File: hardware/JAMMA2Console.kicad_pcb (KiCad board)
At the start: 2 copper layers, 138 x 105 mm, 175 parts, among them J1 Conn_02x28_JAMMA, J10 Conn_02x03_Counter_Clockwise, J11 Conn_02x05_Odd_Even, J2 DB15_Female_HighDensity, J3 SCART-F, J4 DF1BZ-34DP-2.5DSA, J5 Conn_Coaxial_x2, J6 DB15_Female, J7 DB15_Female, J8 Phoenix PTS 1,5/4-5.0, J9 USB_B, U1 USBLC6-2P6, U10 74LVC4245, U11 74LVC4245, U12 TL074, U13 LM1972, U14 TPA3138D2, U15 74HCT4053, U2 LD1117-3.3, U3 74HCT4053, U4 74HCT86, U5 74HCT4053, U6 LM1881, U7 THS7375, U8 STM32F103V8Tx, U9 74LVC4245, Y1 8MHz

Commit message: Completing the functionality of PCB layout. Require silkscreen placement still, though.
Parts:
- removed RN10, RN14, RN3, RN7, RN8, RN9: 10k, Resistor_SMD:R_Array_Convex_4x0603
- added C70: 100n, Capacitor_SMD:C_0603_1608Metric, F.Cu at (157.2, 133.8)
- added C71: 100n, Capacitor_SMD:C_0603_1608Metric, F.Cu at (157.2, 149.7)
- added D7: LESD3Z5.0CMT1G, Diode_SMD:D_SOD-323, F.Cu at (52.9, 157.3)
- added J12: Conn_01x03, Connector_PinHeader_2.54mm:PinHeader_1x03_P2.54mm_Vertical, F.Cu at (106.6, 139.9)
- added JP3: Jumper_NC_Small, Jumper:SolderJumper-2_P1.3mm_Bridged2Bar_Pad1.0x1.5mm, F.Cu at (102.9, 142.5)
- added R30: 1K5, Resistor_SMD:R_0603_1608Metric, F.Cu at (57.6, 156.8)
- added R31: 10K, Resistor_SMD:R_0603_1608Metric, F.Cu at (111.0, 140.7)
- added R32: 10K, Resistor_SMD:R_0603_1608Metric, F.Cu at (123.9, 140.7)
- added R33: 10K, Resistor_SMD:R_0603_1608Metric, F.Cu at (137.0, 140.8)
- added R34: 10K, Resistor_SMD:R_0603_1608Metric, F.Cu at (159.5, 133.0)
- added R35: 10K, Resistor_SMD:R_0603_1608Metric, F.Cu at (159.4, 148.9)
- added R36: 10K, Resistor_SMD:R_Array_Convex_4x0603, F.Cu at (100.9, 104.8)
- added R37: 10K, Resistor_SMD:R_Array_Convex_4x0603, F.Cu at (81.2, 124.7)
- added R38: 10K, Resistor_SMD:R_Array_Convex_4x0603, F.Cu at (85.6, 125.0)
- added R39: 10K, Resistor_SMD:R_Array_Convex_4x0603, F.Cu at (148.5, 99.8)
- added R40: 10K, Resistor_SMD:R_0603_1608Metric, F.Cu at (157.2, 132.2)
- added R41: 10K, Resistor_SMD:R_0603_1608Metric, F.Cu at (157.2, 148.2)
- added R42: 10K, Resistor_SMD:R_0603_1608Metric, F.Cu at (99.2, 126.7)
- added R43: 10K, Resistor_SMD:R_0603_1608Metric, F.Cu at (88.2, 125.0)
- added SW1: SW_Push, Console2JAMMA:SW_Push_SPST_NO_Alps_SKRP, F.Cu at (110.0, 98.8)
- added SW2: SW_Push, Console2JAMMA:SW_Push_SPST_NO_Alps_SKRP, F.Cu at (157.5, 128.5)
- added SW3: SW_Push, Console2JAMMA:SW_Push_SPST_NO_Alps_SKRP, F.Cu at (157.5, 144.5)
- J2: value DB15_Female_HighDensity -> DS1038-15FBNSiA74-0CC; footprint Connector_Dsub:DSUB-15-HD_Female_Horizontal_P2.29x1.98mm_EdgePinOffset8.35mm_Housed_MountingHolesOffset10.89mm -> Console2JAMMA:DSUB-15-HD_Female_Horizontal_P2.29x1.98mm_EdgePinOffset8.63mm_Housed_MountingHolesOffset11.17mm
- J3: footprint Console2JAMMA:Conn_SCART_Female -> Console2JAMMA:Conn_SCART_Female_Right_Angle
- J5: value Conn_Coaxial_x2 -> AudioJack3; footprint Console2JAMMA:RCA_Switchchraft_Dual -> Connector_Audio:Jack_3.5mm_CUI_SJ-3523-SMT_Horizontal
- J6, J7: value DB15_Female -> DS1037-15FNAKT74-0CC; footprint Connector_Dsub:DSUB-15_Female_Horizontal_P2.77x2.84mm_EdgePinOffset7.70mm_Housed_MountingHolesOffset9.12mm -> Console2JAMMA:DSUB-15_Female_Horizontal_P2.77x2.84mm_EdgePinOffset8.10mm_Housed_MountingHolesOffset9.52mm
- J9: value USB_B -> USB_B_Mini; footprint Connector_USB:USB_B_OST_USB-B1HSxx_Horizontal -> Connector_USB:USB_Mini-B_Lumberg_2486_01_Horizontal
- R9: value 10K -> 680K
- Y1: value 8MHz -> 12MHz
- moved R9 305.0 mm to (45.2, 159.2), turned to 180 degrees
- moved C16 262.2 mm to (80.6, 108.7), turned to 90 degrees
- moved C24 243.1 mm to (94.2, 104.5)
- moved C25 239.9 mm to (101.7, 108.3), turned to 270 degrees
- moved C23 238.5 mm to (98.5, 123.8), turned to 180 degrees
- moved C22 237.6 mm to (82.0, 121.2), turned to 90 degrees
- moved C17 234.3 mm to (86.4, 101.7), turned to 180 degrees
- moved C31 234.2 mm to (111.0, 137.6), turned to 270 degrees
- moved RN18 231.5 mm to (115.5, 144.5), turned to 90 degrees
- moved C21 230.9 mm to (82.3, 108.8), turned to 90 degrees
- moved C34 228.6 mm to (112.5, 140.7), turned to 90 degrees
- moved C35 227.1 mm to (125.4, 140.7), turned to 90 degrees
- moved C28 224.7 mm to (112.5, 137.7), turned to 270 degrees
- moved RN21 223.5 mm to (132.5, 144.5), turned to 90 degrees
- moved C20 222.2 mm to (86.4, 103.3), turned to 180 degrees
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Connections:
- net /Audio/Audio_L_Mono renamed /Audio/Audio_~Mono~_L
- net Net-(J9-Pad2) renamed /D-
- net Net-(J9-Pad3) renamed /D+
- C14 pad 1: +3V3 -> +5V
- C15 pad 1: +3V3 -> +5V
- C66 pad 1: /Speaker_JAMMA+ -> /Speaker_JAMMA-
- C67 pad 2: /Speaker_JAMMA- -> /Speaker_JAMMA+
- D8 pad 1: /VGA_HSYNC -> GND
- D8 pad 2: GND -> /VGA_HSYNC
- D9 pad 1: /VGA_VSYNC -> GND
- D9 pad 2: GND -> /VGA_VSYNC
- J2 pad 0: (no net) -> GND
- J6 pad 0: (no net) -> GND
- J6 pad 1: /Digital I/O/VCC -> Net-(J6-Pad1)
- J6 pad 10: /Digital I/O/P1_3 -> /Digital I/O/P1_2
- J6 pad 11: /Digital I/O/P1_5 -> /Digital I/O/P1_4
- J6 pad 12: /Digital I/O/P1_7 -> /Digital I/O/P1_6
- J6 pad 13: /Digital I/O/P1_9 -> /Digital I/O/P1_8
- J6 pad 14: /Digital I/O/P1_11 -> /Digital I/O/P1_10
- J6 pad 15: GND -> /Digital I/O/P1_12
- J6 pad 2: /Digital I/O/P1_2 -> /Digital I/O/P1_1
- J6 pad 3: /Digital I/O/P1_4 -> /Digital I/O/P1_3
- J6 pad 4: /Digital I/O/P1_6 -> /Digital I/O/P1_5
- J6 pad 5: /Digital I/O/P1_8 -> /Digital I/O/P1_7
- J6 pad 6: /Digital I/O/P1_10 -> /Digital I/O/P1_9
- J6 pad 7: /Digital I/O/P1_12 -> /Digital I/O/P1_11
- J6 pad 9: /Digital I/O/P1_1 -> Net-(J6-Pad9)
- J7 pad 0: (no net) -> GND
- J7 pad 1: /Digital I/O/VCC -> Net-(J6-Pad1)
- J7 pad 10: /Digital I/O/P2_3 -> /Digital I/O/P2_2
- J7 pad 11: /Digital I/O/P2_5 -> /Digital I/O/P2_4
- J7 pad 12: /Digital I/O/P2_7 -> /Digital I/O/P2_6
- J7 pad 13: /Digital I/O/P2_9 -> /Digital I/O/P2_8
- J7 pad 14: /Digital I/O/P2_11 -> /Digital I/O/P2_10
- J7 pad 15: GND -> /Digital I/O/P2_12
- J7 pad 2: /Digital I/O/P2_2 -> /Digital I/O/P2_1
- J7 pad 3: /Digital I/O/P2_4 -> /Digital I/O/P2_3
- J7 pad 4: /Digital I/O/P2_6 -> /Digital I/O/P2_5
- J7 pad 5: /Digital I/O/P2_8 -> /Digital I/O/P2_7
- J7 pad 6: /Digital I/O/P2_10 -> /Digital I/O/P2_9
- J7 pad 7: /Digital I/O/P2_12 -> /Digital I/O/P2_11
- J7 pad 9: /Digital I/O/P2_1 -> Net-(J7-Pad9)
- J8 pad 1: /Audio/Speaker_R+ -> /Speaker_JAMMA+
- J8 pad 2: /Audio/Speaker_R- -> /Speaker_JAMMA-
- J8 pad 3: /Speaker_JAMMA- -> /Audio/Speaker_R+
- J8 pad 4: /Speaker_JAMMA+ -> /Audio/Speaker_R-
- J9 pad 4: GND -> Net-(J9-Pad4)
- JP1 pad 3: +3V3 -> +12V
- JP2 pad 3: +3V3 -> +12V
- L1 pad 2: /Speaker_JAMMA+ -> /Speaker_JAMMA-
- L2 pad 2: /Speaker_JAMMA- -> /Speaker_JAMMA+
- R26 pad 1: +3V3 -> +12V
- R9 pad 1: +3V3 -> Net-(J9-Pad6)
- R9 pad 2: Net-(R9-Pad2) -> GND
- RN1 pad 5: /Video/Video_CSYNC -> /Video/Video_Green
- RN1 pad 6: /Video/Video_Blue -> /Video/Video_Red
- RN1 pad 7: /Video/Video_Green -> /Video/Video_CSYNC
- RN1 pad 8: /Video/Video_Red -> /Video/Video_Blue
- RN11 pad 1: /Digital I/O/P1_Shifter_DIR -> Net-(RN11-Pad1)
- RN11 pad 2: /Digital I/O/P1_Button1 -> Net-(RN11-Pad2)
- RN11 pad 3: /Digital I/O/P1_Button2 -> Net-(RN11-Pad3)
- RN11 pad 4: /Digital I/O/P1_Button3 -> Net-(RN11-Pad4)
- RN11 pad 5: Net-(RN11-Pad5) -> /Digital I/O/P1_Button4
- RN11 pad 6: Net-(RN11-Pad6) -> /Digital I/O/P1_Button3
- RN11 pad 7: Net-(RN11-Pad7) -> /Digital I/O/P1_Button2
- RN11 pad 8: Net-(RN11-Pad8) -> /Digital I/O/P1_Button1
- RN12 pad 1: /Digital I/O/P1_Button4 -> Net-(RN12-Pad1)
- RN12 pad 2: /Digital I/O/P1_Button5 -> Net-(RN12-Pad2)
- RN12 pad 3: /Digital I/O/P1_Button6 -> Net-(RN12-Pad3)
- RN12 pad 4: /Digital I/O/P1_Button7 -> Net-(RN12-Pad4)
- RN12 pad 5: Net-(RN12-Pad5) -> /Digital I/O/P1_Button8
- RN12 pad 6: Net-(RN12-Pad6) -> /Digital I/O/P1_Button7
- RN12 pad 7: Net-(RN12-Pad7) -> /Digital I/O/P1_Button6
- RN12 pad 8: Net-(RN12-Pad8) -> /Digital I/O/P1_Button5
- RN13 pad 1: /Digital I/O/P1_Button8 -> Net-(RN13-Pad1)
- RN13 pad 2: /Digital I/O/P1&P2_Shifter_DIR -> Net-(RN13-Pad2)
- RN13 pad 3: /Digital I/O/P1_Button9 -> Net-(RN13-Pad3)
- RN13 pad 4: /Digital I/O/P1_Button10 -> Net-(RN13-Pad4)
- RN13 pad 5: Net-(RN13-Pad5) -> /Digital I/O/P1_Button12
- RN13 pad 6: Net-(RN13-Pad6) -> /Digital I/O/P1_Button11
- RN13 pad 7: Net-(RN13-Pad7) -> /Digital I/O/P1_Button10
- RN13 pad 8: Net-(RN13-Pad8) -> /Digital I/O/P1_Button9
- RN15 pad 1: /Digital I/O/P2_Button11 -> Net-(RN15-Pad1)
- RN15 pad 2: /Digital I/O/P2_Button12 -> Net-(RN15-Pad2)
- RN15 pad 3: /Digital I/O/P2_Shifter_DIR -> Net-(RN15-Pad3)
- RN15 pad 4: /Digital I/O/P2_Button1 -> Net-(RN15-Pad4)
- RN15 pad 5: Net-(RN15-Pad5) -> /Digital I/O/P2_Button4
- RN15 pad 6: Net-(RN15-Pad6) -> /Digital I/O/P2_Button3
- RN15 pad 7: Net-(RN15-Pad7) -> /Digital I/O/P2_Button2
- RN15 pad 8: Net-(RN15-Pad8) -> /Digital I/O/P2_Button1
- RN16 pad 1: /Digital I/O/P2_Button2 -> Net-(RN16-Pad1)
- RN16 pad 2: /Digital I/O/P2_Button3 -> Net-(RN16-Pad2)
- RN16 pad 3: /Digital I/O/P2_Button4 -> Net-(RN16-Pad3)
- RN16 pad 4: /Digital I/O/P2_Button5 -> Net-(RN16-Pad4)
- RN16 pad 5: Net-(RN16-Pad5) -> /Digital I/O/P2_Button8
- RN16 pad 6: Net-(RN16-Pad6) -> /Digital I/O/P2_Button7
- RN16 pad 7: Net-(RN16-Pad7) -> /Digital I/O/P2_Button6
- RN16 pad 8: Net-(RN16-Pad8) -> /Digital I/O/P2_Button5
- RN17 pad 1: /Digital I/O/P2_Button6 -> Net-(RN17-Pad1)
- RN17 pad 2: /Digital I/O/P2_Button7 -> Net-(RN17-Pad2)
- RN17 pad 3: /Digital I/O/P2_Button8 -> Net-(RN17-Pad3)
- RN17 pad 5: Net-(RN17-Pad5) -> /Digital I/O/P2_Button12
- RN17 pad 6: Net-(RN17-Pad6) -> /Digital I/O/P2_Button11
- RN17 pad 7: Net-(RN17-Pad7) -> /Digital I/O/P2_Button10
- RN17 pad 8: Net-(RN17-Pad8) -> /Digital I/O/P2_Button9
- RN18 pad 1: Net-(RN18-Pad1) -> /Digital I/O/P1_1
- RN18 pad 2: Net-(RN18-Pad2) -> /Digital I/O/P1_2
- RN18 pad 3: Net-(RN18-Pad3) -> /Digital I/O/P1_3
- RN18 pad 4: Net-(RN18-Pad4) -> /Digital I/O/P1_4
- RN18 pad 5: /Digital I/O/P1_4 -> Net-(RN18-Pad5)
- RN18 pad 6: /Digital I/O/P1_3 -> Net-(RN18-Pad6)
- RN18 pad 7: /Digital I/O/P1_2 -> Net-(RN18-Pad7)
- RN18 pad 8: /Digital I/O/P1_1 -> Net-(RN18-Pad8)
- RN19 pad 1: Net-(RN19-Pad1) -> /Digital I/O/P1_5
- RN19 pad 2: Net-(RN19-Pad2) -> /Digital I/O/P1_6
- RN19 pad 3: Net-(RN19-Pad3) -> /Digital I/O/P1_7
- RN19 pad 4: Net-(RN19-Pad4) -> /Digital I/O/P1_8
- RN19 pad 5: /Digital I/O/P1_8 -> Net-(RN19-Pad5)
- RN19 pad 6: /Digital I/O/P1_7 -> Net-(RN19-Pad6)
- RN19 pad 7: /Digital I/O/P1_6 -> Net-(RN19-Pad7)
- RN19 pad 8: /Digital I/O/P1_5 -> Net-(RN19-Pad8)
- RN2 pad 5: /Composite_Sync -> /Video_Green
- RN2 pad 6: /Video_Blue -> /Video_Red
- RN2 pad 7: /Video_Green -> /Composite_Sync
- RN2 pad 8: /Video_Red -> /Video_Blue
- RN20 pad 1: Net-(RN20-Pad1) -> /Digital I/O/P1_9
- RN20 pad 2: Net-(RN20-Pad2) -> /Digital I/O/P1_10
- RN20 pad 3: Net-(RN20-Pad3) -> /Digital I/O/P1_11
- RN20 pad 4: Net-(RN20-Pad4) -> /Digital I/O/P1_12
- RN20 pad 5: /Digital I/O/P1_12 -> Net-(RN20-Pad5)
- RN20 pad 6: /Digital I/O/P1_11 -> Net-(RN20-Pad6)
- RN20 pad 7: /Digital I/O/P1_10 -> Net-(RN20-Pad7)
- RN20 pad 8: /Digital I/O/P1_9 -> Net-(RN20-Pad8)
- RN21 pad 1: Net-(RN21-Pad1) -> /Digital I/O/P2_1
- RN21 pad 2: Net-(RN21-Pad2) -> /Digital I/O/P2_2
- RN21 pad 3: Net-(RN21-Pad3) -> /Digital I/O/P2_3
- RN21 pad 4: Net-(RN21-Pad4) -> /Digital I/O/P2_4
- RN21 pad 5: /Digital I/O/P2_12 -> Net-(RN21-Pad5)
- RN21 pad 6: /Digital I/O/P2_11 -> Net-(RN21-Pad6)
- RN21 pad 7: /Digital I/O/P2_10 -> Net-(RN21-Pad7)
- RN21 pad 8: /Digital I/O/P2_9 -> Net-(RN21-Pad8)
- RN22 pad 1: Net-(RN22-Pad1) -> /Digital I/O/P2_5
- RN22 pad 2: Net-(RN22-Pad2) -> /Digital I/O/P2_6
- RN22 pad 3: Net-(RN22-Pad3) -> /Digital I/O/P2_7
- RN22 pad 4: Net-(RN22-Pad4) -> /Digital I/O/P2_8
- RN22 pad 5: /Digital I/O/P2_4 -> Net-(RN22-Pad5)
- RN22 pad 6: /Digital I/O/P2_3 -> Net-(RN22-Pad6)
- RN22 pad 7: /Digital I/O/P2_2 -> Net-(RN22-Pad7)
- RN22 pad 8: /Digital I/O/P2_1 -> Net-(RN22-Pad8)
- RN23 pad 1: Net-(RN23-Pad1) -> /Digital I/O/P2_9
- RN23 pad 2: Net-(RN23-Pad2) -> /Digital I/O/P2_10
- RN23 pad 3: Net-(RN23-Pad3) -> /Digital I/O/P2_11
- RN23 pad 4: Net-(RN23-Pad4) -> /Digital I/O/P2_12
- RN23 pad 5: /Digital I/O/P2_8 -> Net-(RN23-Pad5)
- RN23 pad 6: /Digital I/O/P2_7 -> Net-(RN23-Pad6)
- RN23 pad 7: /Digital I/O/P2_6 -> Net-(RN23-Pad7)
- RN23 pad 8: /Digital I/O/P2_5 -> Net-(RN23-Pad8)
- RN4 pad 1: /P1_Down -> /P1_Start
- RN4 pad 2: /P1_Left -> /P2_Up
- RN4 pad 3: /P1_Right -> /P1_Up
- RN4 pad 4: /P1_A -> /P2_Down
- RN5 pad 1: /P1_B -> /P1_Down
- RN5 pad 2: /P1_C -> /P2_Left
- RN5 pad 3: /P1_X -> /P1_Left
- RN5 pad 4: /P1_Y -> /P2_Right
- RN6 pad 1: /P1_Z -> /P1_Right
- RN6 pad 2: /P1_HK -> /P2_A
- RN6 pad 3: /P1_MK -> /P1_A
- RN6 pad 4: /P1_LK -> /P2_B
- U10 pad 10: Net-(RN21-Pad4) -> Net-(RN21-Pad5)
- U10 pad 14: Net-(RN15-Pad7) -> Net-(RN15-Pad4)
- U10 pad 15: Net-(RN15-Pad8) -> Net-(RN15-Pad3)
- U10 pad 16: Net-(RN14-Pad5) -> Net-(RN15-Pad2)
- U10 pad 17: Net-(RN14-Pad6) -> Net-(RN15-Pad1)
- U10 pad 18: Net-(RN14-Pad7) -> Net-(RN13-Pad4)
- U10 pad 19: Net-(RN14-Pad8) -> Net-(RN13-Pad3)
- U10 pad 2: Net-(RN13-Pad7) -> Net-(R32-Pad1)
- U10 pad 20: Net-(RN13-Pad5) -> Net-(RN13-Pad2)
- U10 pad 21: Net-(RN13-Pad6) -> Net-(RN13-Pad1)
- U10 pad 3: Net-(RN20-Pad1) -> Net-(RN20-Pad8)
- U10 pad 4: Net-(RN20-Pad2) -> Net-(RN20-Pad7)
- U10 pad 5: Net-(RN20-Pad3) -> Net-(RN20-Pad6)
- U10 pad 6: Net-(RN20-Pad4) -> Net-(RN20-Pad5)
- U10 pad 7: Net-(RN21-Pad1) -> Net-(RN21-Pad8)
- U10 pad 8: Net-(RN21-Pad2) -> Net-(RN21-Pad7)
- U10 pad 9: Net-(RN21-Pad3) -> Net-(RN21-Pad6)
- U11 pad 10: Net-(RN23-Pad4) -> Net-(RN23-Pad5)
- U11 pad 14: Net-(RN17-Pad6) -> Net-(RN17-Pad4)
- U11 pad 15: Net-(RN17-Pad7) -> Net-(RN17-Pad3)
- U11 pad 16: Net-(RN17-Pad8) -> Net-(RN17-Pad2)
- U11 pad 17: Net-(RN16-Pad5) -> Net-(RN17-Pad1)
- U11 pad 18: Net-(RN16-Pad6) -> Net-(RN16-Pad4)
- U11 pad 19: Net-(RN16-Pad7) -> Net-(RN16-Pad3)
- U11 pad 2: Net-(RN15-Pad6) -> Net-(R33-Pad1)
- U11 pad 20: Net-(RN16-Pad8) -> Net-(RN16-Pad2)
- U11 pad 21: Net-(RN15-Pad5) -> Net-(RN16-Pad1)
- U11 pad 3: Net-(RN22-Pad1) -> Net-(RN22-Pad8)
- U11 pad 4: Net-(RN22-Pad2) -> Net-(RN22-Pad7)
- U11 pad 5: Net-(RN22-Pad3) -> Net-(RN22-Pad6)
- U11 pad 6: Net-(RN22-Pad4) -> Net-(RN22-Pad5)
- U11 pad 7: Net-(RN23-Pad1) -> Net-(RN23-Pad8)
- U11 pad 8: Net-(RN23-Pad2) -> Net-(RN23-Pad7)
- U11 pad 9: Net-(RN23-Pad3) -> Net-(RN23-Pad6)
- U15 pad 3: /Audio/Audio_Mono -> /Audio/Audio_L
- U15 pad 5: /Audio/Audio_L -> /Audio/Audio_Mono
- U3 pad 1: /VGA_Green -> /VGA_Blue
- U3 pad 2: /SCART_Green -> /SCART_Blue
- U3 pad 3: /VGA_Blue -> /VGA_Green
- U3 pad 5: /SCART_Blue -> /SCART_Green
- U4 pad 10: Net-(U4-Pad10) -> +5V
- U4 pad 11: /Video/VGA_CSYNC -> Net-(U4-Pad11)
- U4 pad 12: +5V -> Net-(U4-Pad12)
- U4 pad 3: Net-(U4-Pad3) -> Net-(U4-Pad13)
- U4 pad 6: Net-(U4-Pad10) -> Net-(U4-Pad12)
- U4 pad 8: Net-(U4-Pad13) -> /Video/VGA_CSYNC
- U4 pad 9: Net-(U4-Pad3) -> Net-(U4-Pad11)
- U7 pad 1: /Video/Video_Red -> /Video/Video_Blue
- U7 pad 10: +3V3 -> +5V
- U7 pad 2: /Video/Video_Green -> /Video/Video_CSYNC
- U7 pad 3: /Video/Video_Blue -> /Video/Video_Red
- U7 pad 4: /Video/Video_CSYNC -> /Video/Video_Green
- U8 pad 14: Net-(R9-Pad2) -> Net-(R36-Pad8)
- U8 pad 15: /Digital I/O/P2_Shifter_DIR -> /VOL_DATA_IN
- U8 pad 16: /Digital I/O/P2_Button11 -> /VOL_LOAD_SHIFT
- U8 pad 17: /Digital I/O/P2_Button12 -> /VOL_CLK
- U8 pad 18: /VOL_CLK -> Net-(U8-Pad18)
- U8 pad 23: /Digital I/O/P1_Shifter_DIR -> /Audio_Select_L
- U8 pad 24: /Digital I/O/P1_Button1 -> /Audio_Select_R
- U8 pad 25: /Digital I/O/P1_Button2 -> /Audio_Select_Mono
- U8 pad 26: /Digital I/O/P1_Button3 -> /Video_Select_CSYNC
- U8 pad 29: /Digital I/O/P1_Button4 -> /Video_Select_Green
- U8 pad 30: /Digital I/O/P1_Button5 -> /Video_Select_Blue
- U8 pad 31: /Digital I/O/P1_Button6 -> /Video_Select_Red
- U8 pad 32: /Digital I/O/P1_Button7 -> /Digital I/O/Volume_Down
- U8 pad 33: /VOL_LOAD_SHIFT -> /Digital I/O/Volume_Up
- U8 pad 34: /VOL_DATA_IN -> /Digital I/O/P1_Shifter_DIR
- U8 pad 36: /Digital I/O/P1_Button11 -> /Digital I/O/P2_Shifter_DIR
- U8 pad 47: /Digital I/O/P2_Button5 -> Net-(R37-Pad2)
- U8 pad 48: /Digital I/O/P2_Button6 -> Net-(R37-Pad3)
- U8 pad 51: /Digital I/O/P2_Button7 -> Net-(R37-Pad1)
- U8 pad 52: /Digital I/O/P2_Button8 -> Net-(R38-Pad4)
- U8 pad 53: /Digital I/O/P2_Button9 -> Net-(R38-Pad3)
- U8 pad 54: /Digital I/O/P2_Button10 -> Net-(R38-Pad2)
- U8 pad 57: Net-(RN9-Pad6) -> /Digital I/O/P1_Button1
- U8 pad 58: Net-(RN9-Pad5) -> /Digital I/O/P1_Button2
- U8 pad 59: Net-(RN10-Pad8) -> /Digital I/O/P1_Button3
- U8 pad 6: Net-(U8-Pad6) -> +3V3
- U8 pad 60: Net-(RN10-Pad7) -> /Digital I/O/P1_Button4
- U8 pad 61: Net-(RN10-Pad6) -> /Digital I/O/P1_Button5
- U8 pad 62: Net-(U8-Pad62) -> /Digital I/O/P1_Button6
- U8 pad 63: /Audio_Select_L -> /Digital I/O/P1_Button7
- U8 pad 64: /Audio_Select_R -> /Digital I/O/P1_Button8
- U8 pad 65: /Audio_Select_Mono -> /Digital I/O/P1_Button9
- U8 pad 66: /Video_Select_Red -> /Digital I/O/P1_Button10
- U8 pad 67: /Digital I/O/P1_Button8 -> /Digital I/O/P1_Button11
- U8 pad 68: /Digital I/O/P1_Button9 -> /Digital I/O/P1_Button12
- U8 pad 69: /Digital I/O/P1_Button10 -> /Digital I/O/P2_Button1
- U8 pad 7: Net-(U8-Pad7) -> /P2_LK
- U8 pad 78: /Video_Select_Green -> /Digital I/O/P2_Button2
- U8 pad 79: /Video_Select_Blue -> /Digital I/O/P2_Button3
- U8 pad 8: Net-(U8-Pad8) -> /P2_MK
- U8 pad 80: /Video_Select_CSYNC -> /Digital I/O/P2_Button4
- U8 pad 81: Net-(RN7-Pad8) -> /Digital I/O/P2_Button5
- U8 pad 82: Net-(RN7-Pad7) -> /Digital I/O/P2_Button6
- U8 pad 83: Net-(RN7-Pad6) -> /Digital I/O/P2_Button7
- U8 pad 84: Net-(RN7-Pad5) -> /Digital I/O/P2_Button8
- U8 pad 85: Net-(RN8-Pad8) -> /Digital I/O/P2_Button9
- U8 pad 86: Net-(RN8-Pad7) -> /Digital I/O/P2_Button10
- U8 pad 87: Net-(RN8-Pad6) -> /Digital I/O/P2_Button11
- U8 pad 88: Net-(RN8-Pad5) -> /Digital I/O/USB_Detect
- U8 pad 91: /Digital I/O/P1_Button12 -> /Digital I/O/P2_Button12
- U8 pad 92: /Digital I/O/P2_Button1 -> Net-(R39-Pad4)
- U8 pad 93: /Digital I/O/P2_Button2 -> Net-(R39-Pad3)
- U8 pad 95: /Digital I/O/P2_Button3 -> Net-(R39-Pad2)
- U8 pad 96: /Digital I/O/P2_Button4 -> Net-(R39-Pad1)
- U9 pad 10: Net-(RN19-Pad4) -> Net-(RN19-Pad5)
- U9 pad 14: Net-(RN13-Pad8) -> Net-(RN12-Pad4)
- U9 pad 15: Net-(RN12-Pad5) -> Net-(RN12-Pad3)
- U9 pad 16: Net-(RN12-Pad6) -> Net-(RN12-Pad2)
- U9 pad 17: Net-(RN12-Pad7) -> Net-(RN12-Pad1)
- U9 pad 18: Net-(RN12-Pad8) -> Net-(RN11-Pad4)
- U9 pad 19: Net-(RN11-Pad5) -> Net-(RN11-Pad3)
- U9 pad 2: Net-(RN11-Pad8) -> Net-(R31-Pad1)
- U9 pad 20: Net-(RN11-Pad6) -> Net-(RN11-Pad2)
- U9 pad 21: Net-(RN11-Pad7) -> Net-(RN11-Pad1)
- U9 pad 3: Net-(RN18-Pad1) -> Net-(RN18-Pad8)
- U9 pad 4: Net-(RN18-Pad2) -> Net-(RN18-Pad7)
- U9 pad 5: Net-(RN18-Pad3) -> Net-(RN18-Pad6)
- U9 pad 6: Net-(RN18-Pad4) -> Net-(RN18-Pad5)
- U9 pad 7: Net-(RN19-Pad1) -> Net-(RN19-Pad8)
- U9 pad 8: Net-(RN19-Pad2) -> Net-(RN19-Pad7)
- U9 pad 9: Net-(RN19-Pad3) -> Net-(RN19-Pad6)
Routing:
- net GND: track 87.1 -> 265.9 mm, vias 7 -> 272
- net /P1_B: track 0.00 -> 157.2 mm
- net +5V: track 27.9 -> 169.0 mm, vias 1 -> 35
- net /P1_Z: track 0.00 -> 127.3 mm
- net /Digital I/O/Volume_Up: track 0.00 -> 125.7 mm, vias 0 -> 2
- net /P2_Z: track 0.00 -> 124.6 mm, vias 0 -> 1
- net /P1_Y: track 0.00 -> 120.6 mm
- net /VGA_Green: track 3.70 -> 123.8 mm, vias 0 -> 2
- net /Audio/EXT_Audio_R: track 0.00 -> 119.4 mm, vias 0 -> 4
- net /P2_Y: track 0.00 -> 118.8 mm, vias 0 -> 1
- net /VGA_Red: track 3.70 -> 120.6 mm, vias 0 -> 2
- net /Digital I/O/Volume_Down: track 0.00 -> 115.7 mm, vias 0 -> 2
- net /SCART_Audio_L: track 8.08 -> 123.6 mm, vias 0 -> 4
- net /VGA_Blue: track 3.70 -> 118.9 mm, vias 0 -> 2
- net /P1_X: track 0.00 -> 114.5 mm
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- added copper zone on B.Cu, net +12V
- added copper zone on F.Cu, net +12V
- added copper zone on In2.Cu, net +12V
- added copper zone on F.Cu, net +3V3
- added copper zone on In2.Cu, net +3V3
- added copper zone on B.Cu, net +5V
- added copper zone on F.Cu, net +5V
- added copper zone on In2.Cu, net +5V
- added copper zone on B.Cu, net -5V
- added copper zone on F.Cu, net -5V
- added copper zone on In2.Cu, net -5V
- added copper zone on B.Cu, net GND
- added copper zone on F.Cu, net GND
- added copper zone on In1.Cu, net GND
- added copper zone on F.Cu, net Net-(J9-Pad6)
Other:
- board size 138 x 105 mm -> 126 x 131.5 mm
- copper layers 2 -> 4
- net class Default: via_dia 0.8 -> 0.7; via_drill 0.4 -> 0.3
- board text added: "3.3V"
- board text added: "5V"
- board text added: "CPS2 Kick Harness"
- board text added: "Down"
- board text added: "SCART Video & Audio"
- board text added: "USB"
- board text added: "Up"
- board text added: "Volume"
- board text removed: "28"
- board text removed: "SCART Input"
- board text removed: "Speaker Out"
- board text removed: "f"

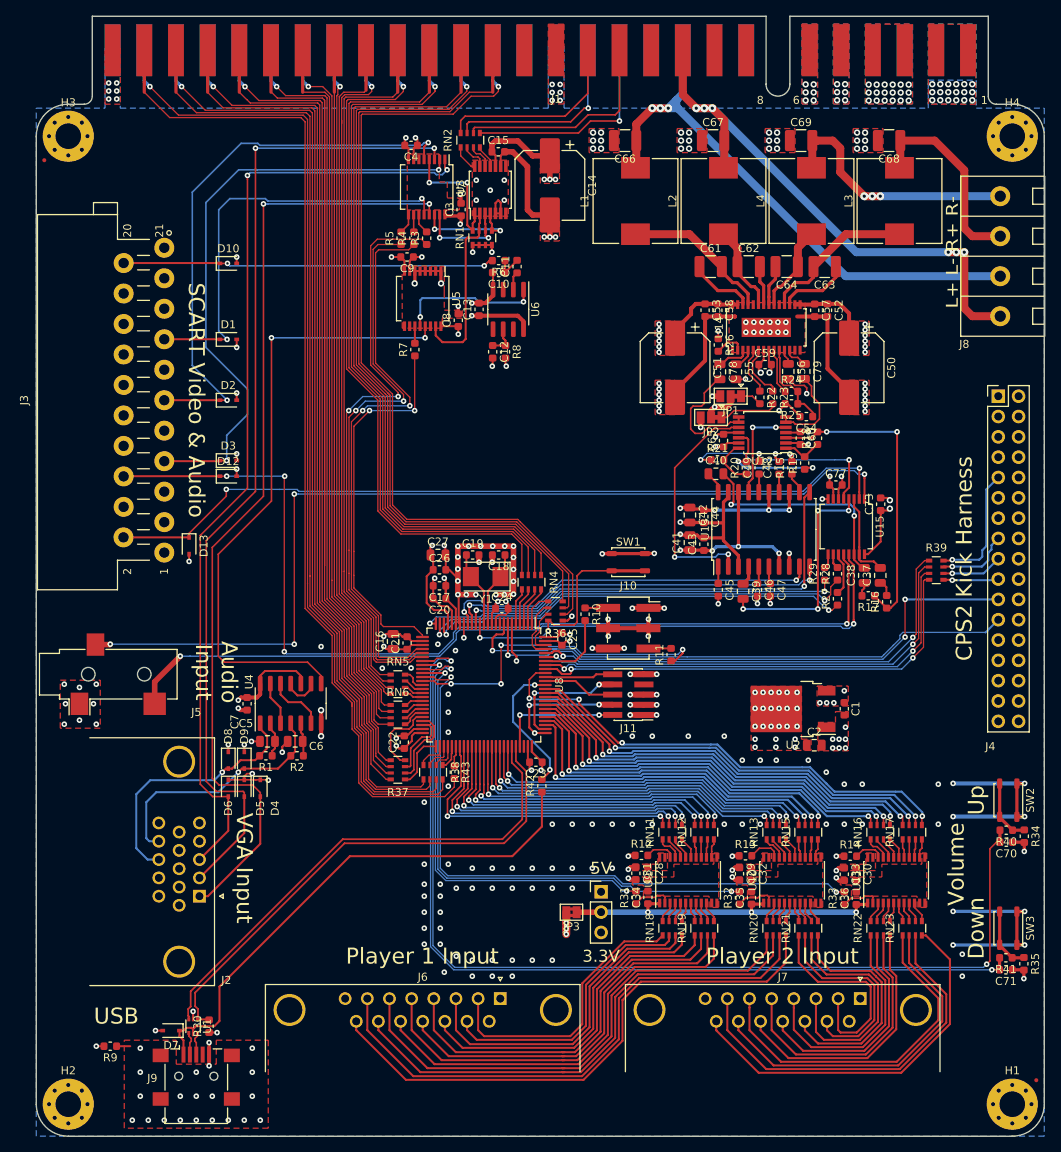
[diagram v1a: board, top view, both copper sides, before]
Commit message: Updating silkscreen placement and fixing up a few issues with layout. Still require via stitching to be done. Adding CERN OHL S license in hardware folder.
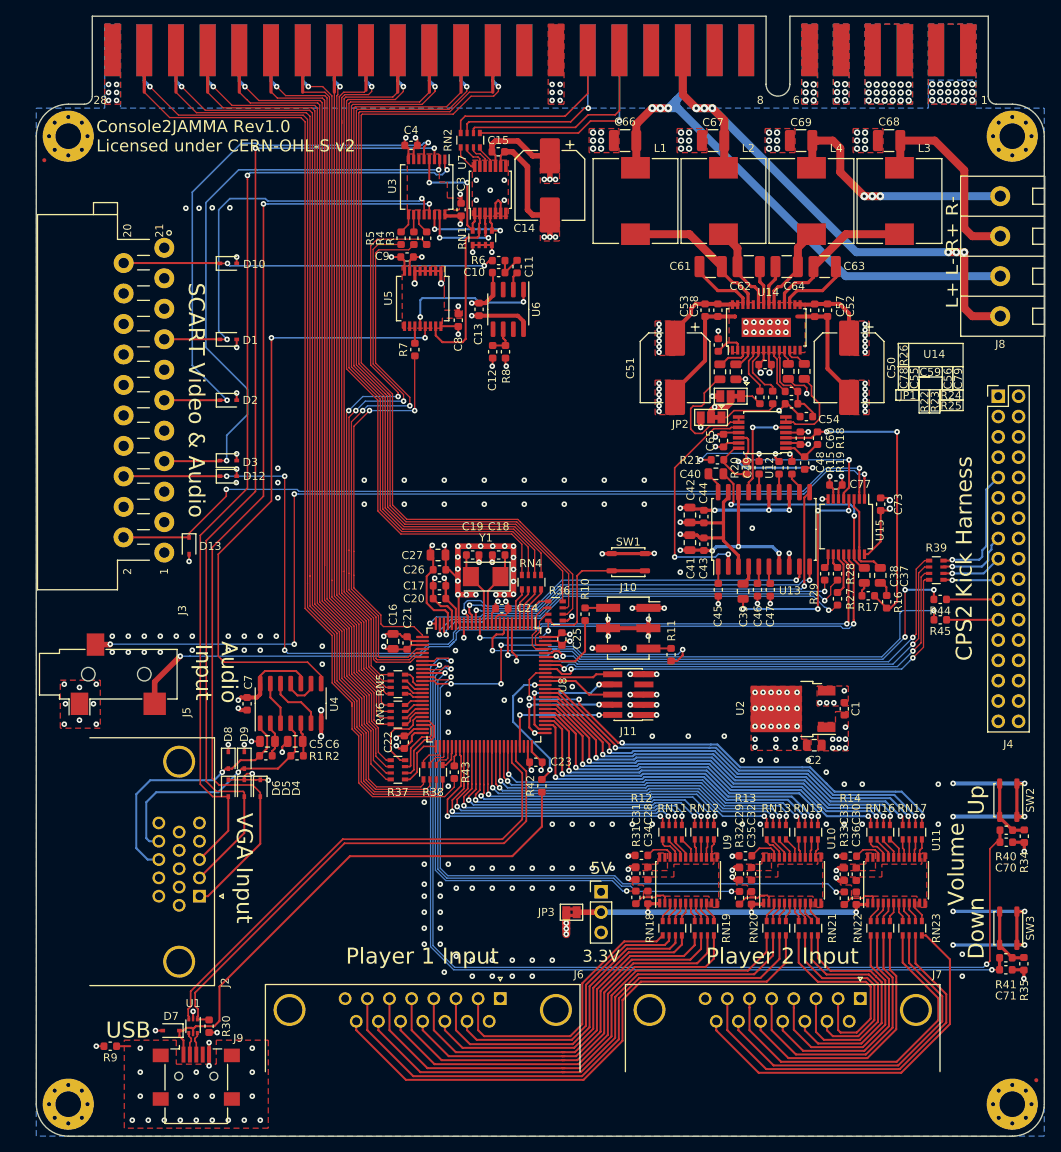
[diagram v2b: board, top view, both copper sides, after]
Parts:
- added R44: 10K, Resistor_SMD:R_0603_1608Metric, F.Cu at (149.0, 103.4)
- added R45: 10K, Resistor_SMD:R_0603_1608Metric, F.Cu at (149.0, 106.0)
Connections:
- U8 pad 7: /P2_LK -> Net-(R44-Pad2)
- U8 pad 8: /P2_MK -> Net-(R45-Pad2)
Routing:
- net Net-(R45-Pad2): track 0.00 -> 66.1 mm, vias 0 -> 2
- net Net-(R44-Pad2): track 0.00 -> 66.1 mm, vias 0 -> 4
- net /P2_LK: track 71.7 -> 6.47 mm, vias 3 -> 0
- net /P2_MK: track 70.9 -> 6.47 mm, vias 1 -> 0
- net /Audio/EXT_Audio_L: track 102.9 -> 103.8 mm
- net GND: vias 272 -> 319
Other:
- board text added: "28"
- board text added: "Console2JAMMA Rev1.0 Licensed under CERN-OHL-S v2"
- board text added: "U14"
- board text added: "f"

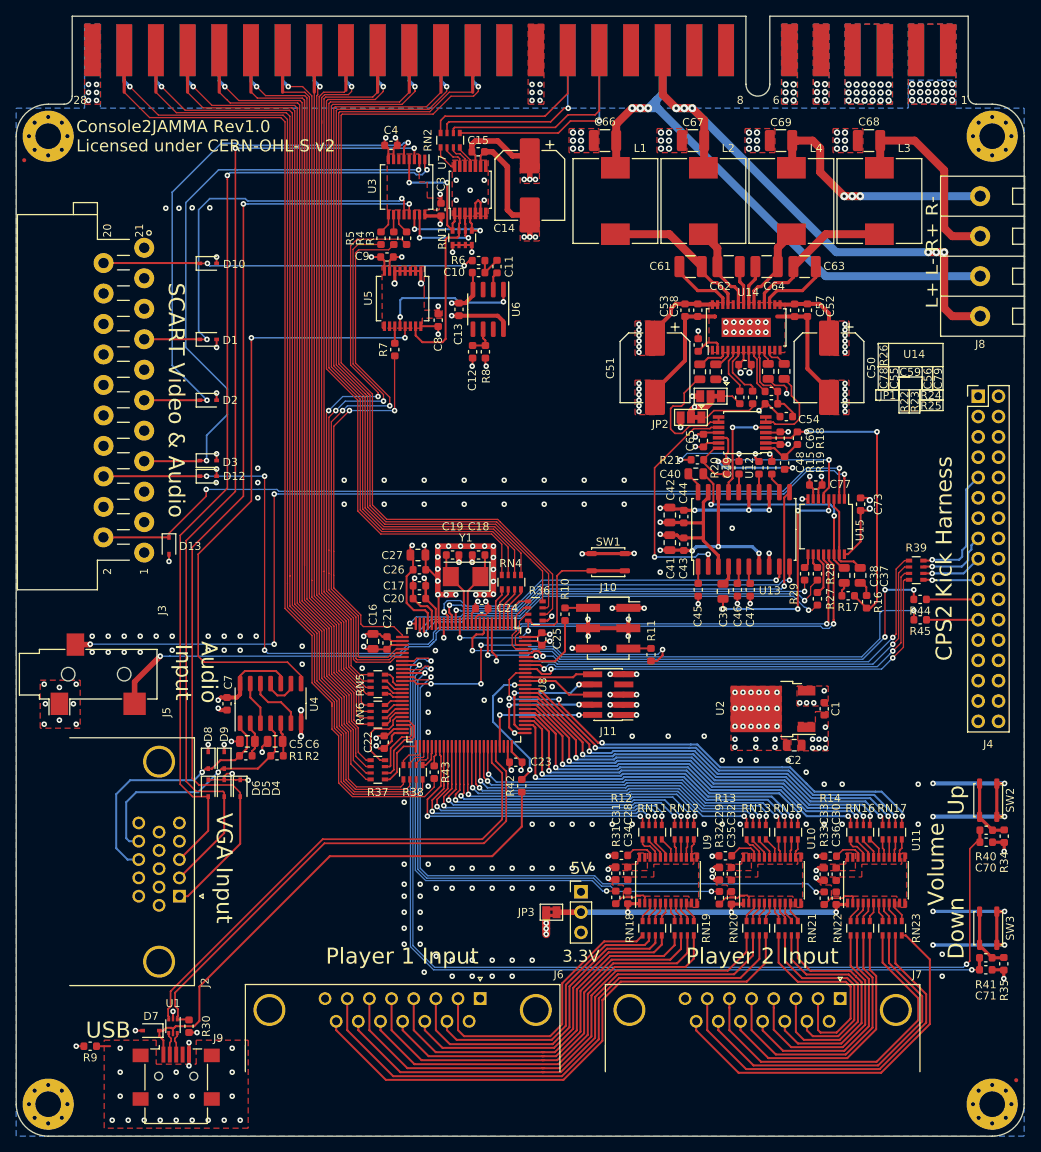
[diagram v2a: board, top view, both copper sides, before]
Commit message: Completing layout & minor edits for the main PCB. Added a project for the adapters to plug controllers into.
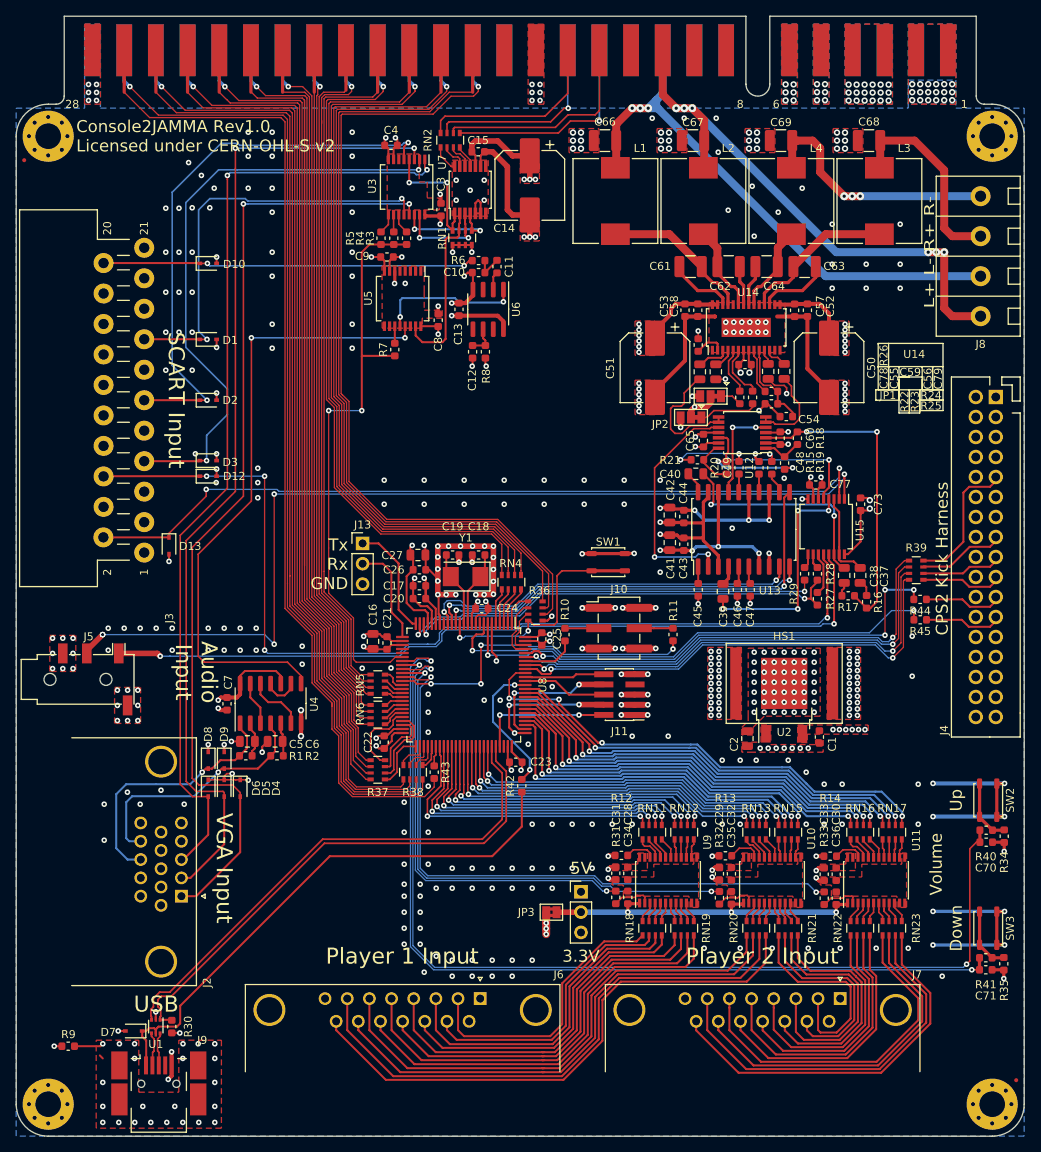
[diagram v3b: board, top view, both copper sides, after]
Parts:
- added HS1: 573100D00010G, Console2JAMMA:Heatsink_AAVID_573100D000x0G_TO-252, F.Cu at (132.0, 113.9)
- added J13: Conn_01x03, Connector_PinHeader_2.54mm:PinHeader_1x03_P2.54mm_Vertical, F.Cu at (79.3, 96.4)
- J10: value Conn_02x03_Counter_Clockwise -> Conn_02x03_Odd_Even; footprint Connector_PinSocket_2.54mm:PinSocket_2x03_P2.54mm_Vertical_SMD -> Connector_PinHeader_2.54mm:PinHeader_2x03_P2.54mm_Vertical_SMD
- J3: footprint Console2JAMMA:Conn_SCART_Female_Right_Angle -> Console2JAMMA:Conn_SCART_CS-107_Right_Angle_Female
- J4: footprint Connector_PinHeader_2.54mm:PinHeader_2x17_P2.54mm_Vertical -> Console2JAMMA:Conn_02x17_DF1BZ-34DP-2.5DSA
- J5: value AudioJack3 -> PJ-320D; footprint Connector_Audio:Jack_3.5mm_CUI_SJ-3523-SMT_Horizontal -> Connector_Audio:Jack_3.5mm_PJ320D_Horizontal
- J9: value USB_B_Mini -> Molex 67503-1020; footprint Connector_USB:USB_Mini-B_Lumberg_2486_01_Horizontal -> Console2JAMMA:USB_Mini-B_Molex_657031020_Horizontal
- moved J4 20.1 mm to (157.2, 98.1), turned to 90 degrees
- moved C2 5.91 mm to (127.4, 120.8), turned to 270 degrees
- moved R11 3.73 mm to (118.1, 107.8)
- moved C1 3.58 mm to (136.4, 120.6)
- moved J9 3.24 mm to (53.8, 165.4), turned to 180 degrees
- moved R9 2.75 mm to (42.5, 159.2)
- moved R10 2.55 mm to (104.6, 107.8)
- moved R30 2.15 mm to (55.5, 156.8)
- moved U1 2.15 mm to (53.5, 156.8)
- moved D7 2.15 mm to (50.7, 157.3)
- moved U2 1.78 mm to (132.0, 116.0), turned to 90 degrees
- moved J11 1.40 mm to (111.4, 115.3)
- moved J10 1.35 mm to (111.3, 107.0)
- moved J5 0.65 mm to (45.0, 113.4), turned to 0 degrees
- moved J2 0.25 mm to (55.2, 140.5)
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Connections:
- J10 pad 2: Net-(J10-Pad2) -> +3V3
- J10 pad 3: GND -> Net-(J10-Pad3)
- J10 pad 4: GND -> Net-(J10-Pad4)
- J10 pad 5: Net-(J10-Pad5) -> GND
- J10 pad 6: +3V3 -> GND
- R10 pad 1: Net-(J10-Pad2) -> Net-(J10-Pad3)
- R11 pad 2: Net-(J10-Pad5) -> Net-(J10-Pad4)
- R27 pad 1: /Audio_Select_L -> /Audio_Select_~SCART~_EXT
- R28 pad 1: /Audio_Select_R -> /Audio_Select_~SCART~_EXT
- R29 pad 1: /Audio_Select_Mono -> /Audio_Select_~Mono~_Stereo
- R3 pad 1: /Video_Select_Red -> /Video_Select_~SCART~_VGA
- R4 pad 1: /Video_Select_Green -> /Video_Select_~SCART~_VGA
- R5 pad 1: /Video_Select_Blue -> /Video_Select_~SCART~_VGA
- R7 pad 1: /Video_Select_CSYNC -> /Video_Select_~SCART~_VGA
- U5 pad 1: GND -> Net-(U5-Pad1)
- U5 pad 2: GND -> Net-(U5-Pad2)
- U5 pad 3: GND -> Net-(U5-Pad3)
- U5 pad 5: GND -> Net-(U5-Pad5)
- U8 pad 23: /Audio_Select_L -> /Audio_Select_~SCART~_EXT
- U8 pad 24: /Audio_Select_R -> /Audio_Select_~Mono~_Stereo
- U8 pad 25: /Audio_Select_Mono -> /Digital I/O/UART_TX
- U8 pad 26: /Video_Select_CSYNC -> /Digital I/O/UART_RX
- U8 pad 29: /Video_Select_Green -> Net-(U8-Pad29)
- U8 pad 30: /Video_Select_Blue -> Net-(U8-Pad30)
- U8 pad 31: /Video_Select_Red -> /Video_Select_~SCART~_VGA
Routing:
- net /Video_Select_Red: track 73.9 -> 0.00 mm, vias 2 -> 0
- net /Video_Select_~SCART~_VGA: track 0.00 -> 73.0 mm, vias 0 -> 2
- net /Video_Select_Green: track 70.9 -> 0.00 mm, vias 2 -> 0
- net /Video_Select_Blue: track 69.7 -> 0.00 mm, vias 2 -> 0
- net /Audio_Select_~SCART~_EXT: track 0.00 -> 56.0 mm, vias 0 -> 2
- net /Audio_Select_R: track 55.5 -> 0.00 mm, vias 2 -> 0
- net /Audio_Select_L: track 53.7 -> 0.00 mm, vias 2 -> 0
- net /Audio_Select_~Mono~_Stereo: track 0.00 -> 53.4 mm, vias 0 -> 2
- net /Audio_Select_Mono: track 53.2 -> 0.00 mm, vias 2 -> 0
- net /Video_Select_CSYNC: track 47.4 -> 0.00 mm, vias 2 -> 0
- net /Digital I/O/UART_TX: track 0.00 -> 14.2 mm
- net /Digital I/O/UART_RX: track 0.00 -> 12.7 mm
- net Net-(J10-Pad3): track 0.00 -> 4.23 mm
- net Net-(J10-Pad4): track 0.00 -> 4.23 mm
- net GND: track 265.9 -> 261.9 mm, vias 319 -> 435
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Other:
- outline, holes or cut-outs redrawn
- board text added: "SCART Input"
- board text added: "Tx Rx GND"
- board text removed: "SCART Video & Audio"
